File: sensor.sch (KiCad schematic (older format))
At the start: 89 parts, among them CON1 Micro USB, CON2 PROG, CON3 Jack-DC, CON4 HTU21D, CON5 Conn_01x08, Q1 BSS214N, Q2 BSS214N, Q3 BSS214N, SW1 RESET, SW2 CFG, U1 LM7805, U2 TLV1117LV33DCY, U3 ESP-12F, U4 HTU21D, U5 PMS7003

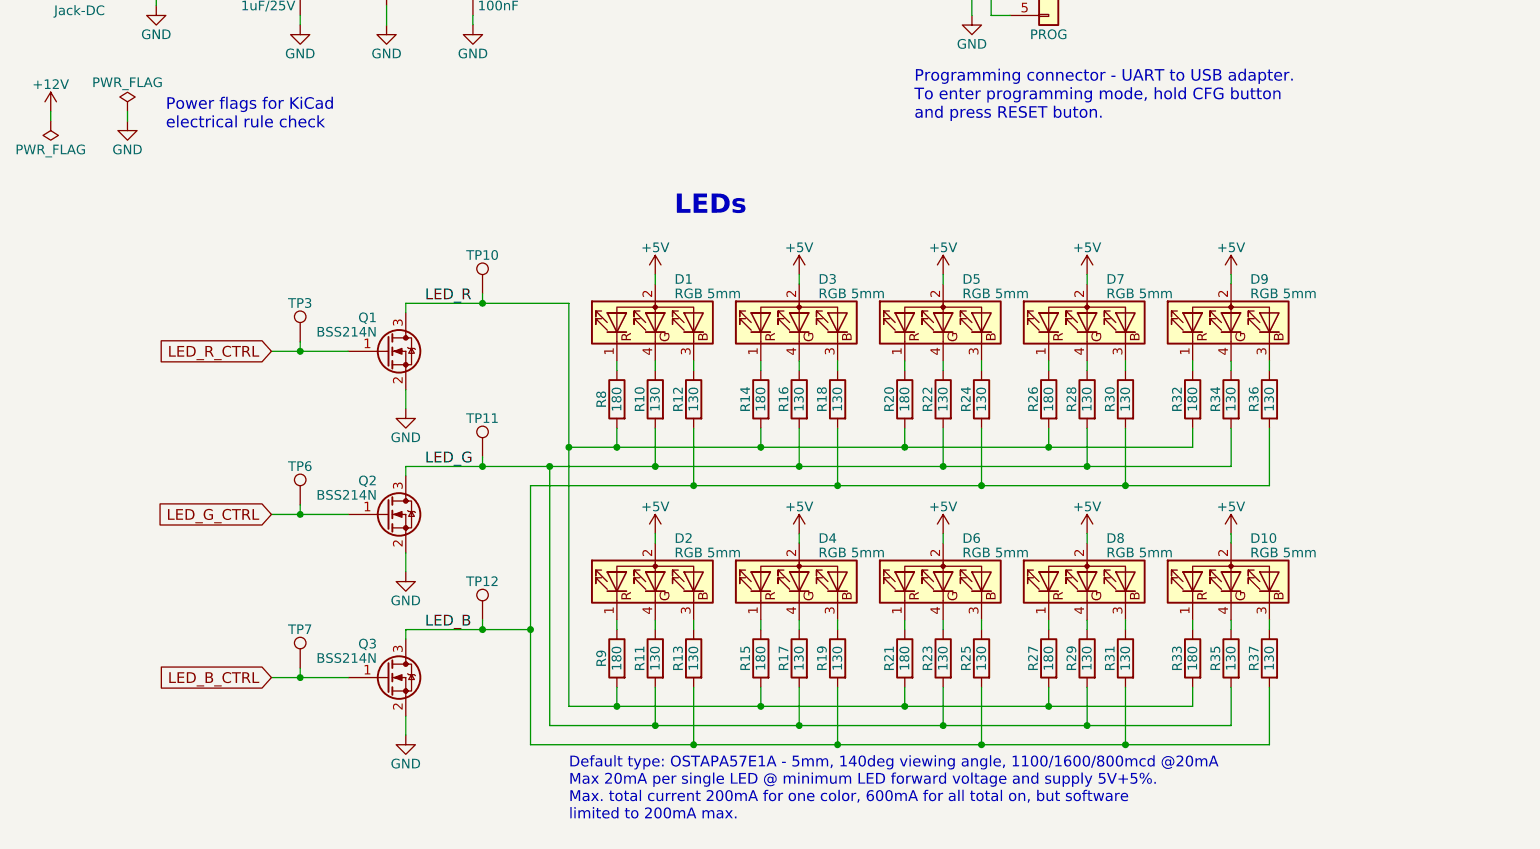
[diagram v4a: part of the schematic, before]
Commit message: [#2] Change LED resistors to chip arrays.
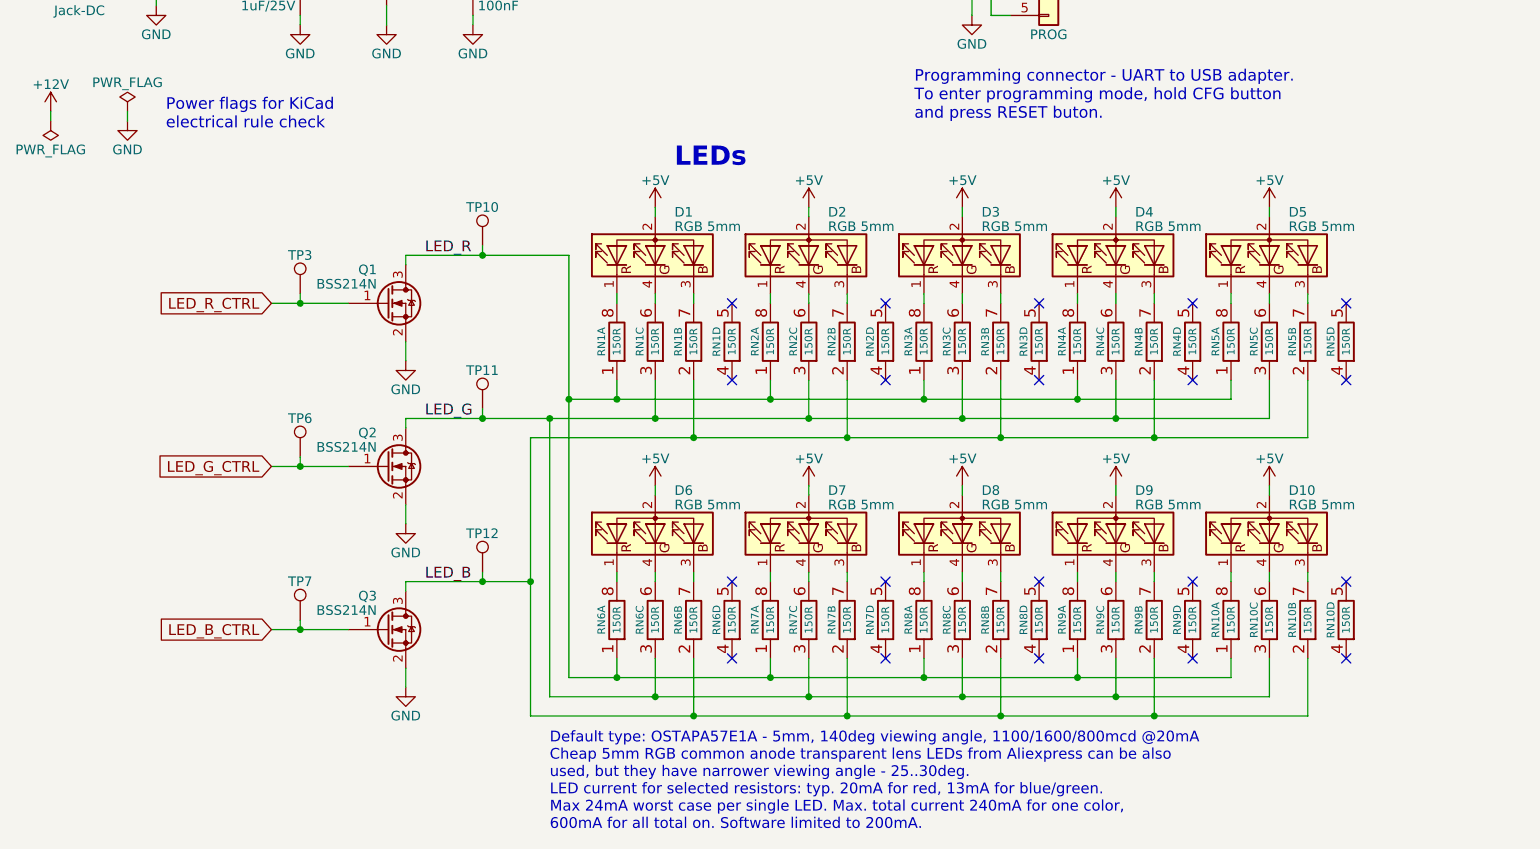
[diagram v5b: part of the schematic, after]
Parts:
- removed R10, R11, R12, R13, R16, R17, R18, R19, R22, R23, R24, R25, R28, R29, R30, R31, R34, R35, R36, R37: 130, less-smog:R_1206, symbol R
- removed R14, R15, R20, R21, R26, R27, R32, R33, R8, R9: 180, less-smog:R_1206, symbol R
- added RN1, RN10, RN2, RN3, RN4, RN5, RN6, RN7, RN8, RN9: 150R, 4x0603_N, symbol R_Network_4
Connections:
- net LED_B: now also RN1.2 (1), RN10.2 (1), RN2.2 (1), RN3.2 (1), RN4.2 (1), RN5.2 (1), RN6.2 (1), RN7.2 (1), RN8.2 (1), RN9.2 (1)
- net LED_G: now also RN1.3 (1), RN10.3 (1), RN2.3 (1), RN3.3 (1), RN4.3 (1), RN5.3 (1), RN6.3 (1), RN7.3 (1), RN8.3 (1), RN9.3 (1)
- net LED_R: now also RN1.1, RN10.1, RN2.1, RN3.1, RN4.1, RN5.1, RN6.1, RN7.1, RN8.1, RN9.1
- net at D1.1 (RK): now also RN1.8 (2)
- net at D1.4 (GK): now also RN1.6 (2)
- net at D1.3 (BK): now also RN1.7 (2)
- net at D3.1 (RK): now also RN3.8 (2)
- net at D3.4 (GK): now also RN3.6 (2)
- net at D3.3 (BK): now also RN3.7 (2)
- net at D5.1 (RK): now also RN5.8 (2)
- net at D5.4 (GK): now also RN5.6 (2)
- net at D5.3 (BK): now also RN5.7 (2)
- net at D7.1 (RK): now also RN7.8 (2)
- net at D7.4 (GK): now also RN7.6 (2)
- net at D7.3 (BK): now also RN7.7 (2)
- net at D9.1 (RK): now also RN9.8 (2)
- net at D9.4 (GK): now also RN9.6 (2)
- net at D9.3 (BK): now also RN9.7 (2)
- net at D2.1 (RK): now also RN2.8 (2)
- net at D2.4 (GK): now also RN2.6 (2)
- net at D2.3 (BK): now also RN2.7 (2)
- net at D4.1 (RK): now also RN4.8 (2)
- net at D4.4 (GK): now also RN4.6 (2)
- net at D4.3 (BK): now also RN4.7 (2)
- net at D6.1 (RK): now also RN6.8 (2)
- net at D6.4 (GK): now also RN6.6 (2)
- net at D6.3 (BK): now also RN6.7 (2)
- net at D8.1 (RK): now also RN8.8 (2)
- net at D8.4 (GK): now also RN8.6 (2)
- net at D8.3 (BK): now also RN8.7 (2)
- net at D10.1 (RK): now also RN10.8 (2)
- net at D10.4 (GK): now also RN10.6 (2)
- net at D10.3 (BK): now also RN10.7 (2)
- no-connect marks 11 -> 31
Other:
- note added: "Default type: OSTAPA57E1A - 5mm, 140deg viewing angle, 1100/1600/800mcd @20mA\nCheap 5mm RGB common anode transparent lens LEDs from Aliexpress can be also\nused, but they have narrower viewing angle - 25..30deg.\nLED current for selected resistors: typ. 20mA for red, 13mA for blue/green.\nMax 24mA worst case per single LED. Max. total current 240mA for one color, \n600mA for all total on. Softwa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"
- note removed: "Default type: OSTAPA57E1A - 5mm, 140deg viewing angle, 1100/1600/800mcd @20mA\nMax 20mA per single LED @ minimum LED forward voltage and supply 5V+5%.\nMax. total current 200mA for one color, 600mA for all total on, but software\nlimited to 200mA max."
- moved on the sheet: D1, D10, D2, D3, D4, D5, D6, D7, D8, D9, Q1, Q2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

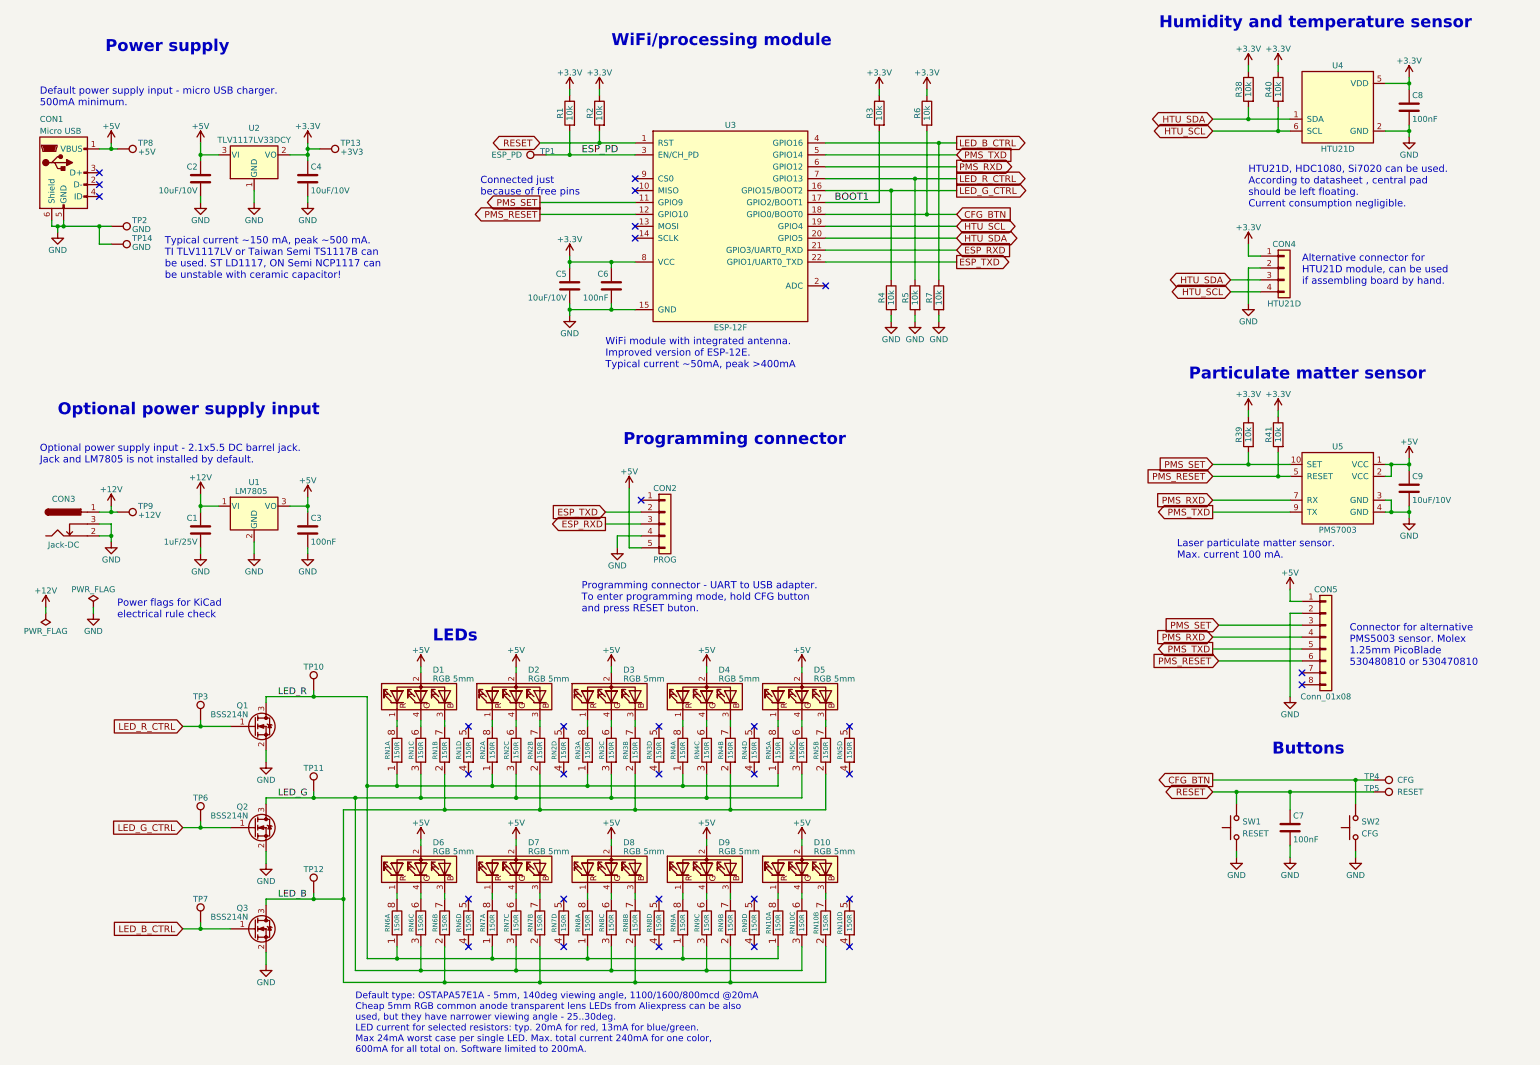
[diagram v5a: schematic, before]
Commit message: Change ESP connections. [#6] Free hardware SPI for Lora module [#9] Disconnect PMS_SET and PMS_RESET Other connections are also moved. ESP programming serial port merged with PMS serial.
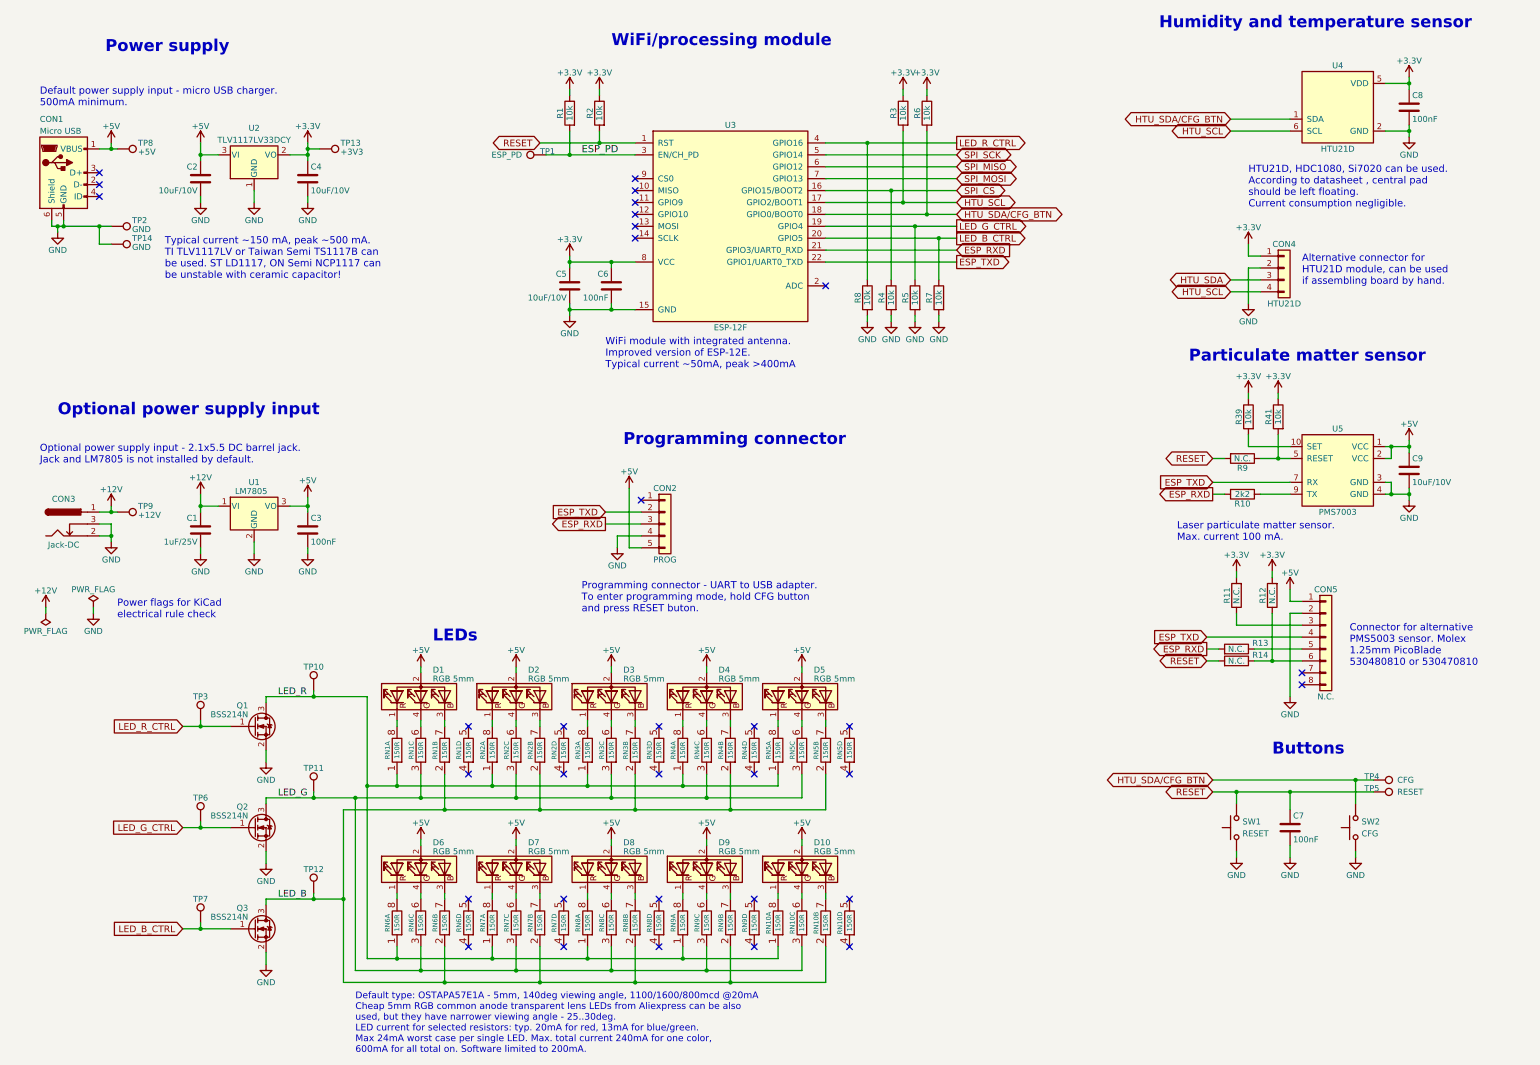
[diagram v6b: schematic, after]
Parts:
- removed R38, R40: 10k, less-smog:R_1206, symbol R
- added R10: 2k2, less-smog:R_1206, symbol R
- added R11, R12, R13, R14, R9: N.C., less-smog:R_1206, symbol R
- added R8: 10k, less-smog:R_1206, symbol R
- CON5: value Conn_01x08 -> N.C.
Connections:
- net BOOT1 is gone; now on net HTU_SCL: R3.2, U3.17 (GPIO2/BOOT1)
- net +3V3: now also R11.2, R12.2
- net ESP_RXD: now also R10.2, R13.2
- net ESP_TXD: now also CON5.4 (Pin_4), U5.7 (RX)
- net GND: now also R8.2
- net HTU_SCL: no longer U3.19 (GPIO4)
- net HTU_SDA: no longer U3.20 (GPIO5), U4.1 (SDA)
- net LED_B_CTRL: now also U3.20 (GPIO5); no longer U3.4 (GPIO16)
- net LED_G_CTRL: now also R5.1, U3.19 (GPIO4); no longer R4.1, U3.16 (GPIO15/BOOT2)
- net LED_R_CTRL: now also U3.4 (GPIO16), R8.1; no longer R5.1, U3.7 (GPIO13)
- net RESET: now also R14.2, R9.2
- net CFG_BTN renamed HTU_SDA/CFG_BTN
- net HTU_SDA/CFG_BTN: now also U4.1 (SDA)
- net PMS_RESET: no longer names the net of R41.2, U5.5 (RESET)
- net PMS_RESET: now also R9.1; no longer CON5.6 (Pin_6), U3.12 (GPIO10)
- removed net PMS_RXD: CON5.4 (Pin_4), U3.6 (GPIO12), U5.7 (RX)
- net PMS_SET: no longer names the net of R39.2, U5.10 (SET)
- net PMS_SET: no longer CON5.3 (Pin_3), U3.11 (GPIO9)
- removed net PMS_TXD: CON5.5 (Pin_5), U3.5 (GPIO14), U5.9 (TX)
- new net: R10.1, U5.9 (TX)
- new net: CON5.3 (Pin_3), R11.1
- new net: CON5.5 (Pin_5), R13.1
- new net: CON5.6 (Pin_6), R12.1, R14.1
- new net SPI_CS: R4.1, U3.16 (GPIO15/BOOT2)
- new net SPI_MISO: U3.6 (GPIO12)
- new net SPI_MOSI: U3.7 (GPIO13)
- new net SPI_SCK: U3.5 (GPIO14)
- no-connect marks 31 -> 33
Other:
- note removed: "Connected just \nbecause of free pins"
- moved on the sheet: C9, R3, R39, R41, U5
